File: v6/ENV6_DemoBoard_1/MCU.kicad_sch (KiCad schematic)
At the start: 50 parts, among them J101 Conn_01x03_Pin, J102 Conn_01x20_Pin, J103 Conn_01x20_Pin, U101 RP235xB, U102 W25Q16JVUXIQ, U103 Pi-Radio, Y101 KX7_QRZ

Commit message: ENV6 (test): Changes after first review
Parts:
- removed C118, C119: 0.1uF, Capacitor_SMD:C_0402_1005Metric, symbol passive:C0402
- removed D102, D103: WS2812B, LED_SMD:LED_WS2812B_PLCC4_5.0x5.0mm_P3.2mm, symbol LED:WS2812B
- removed J101: Conn_01x03_Pin, Connector_PinSocket_2.54mm:PinSocket_1x03_P2.54mm_Vertical, symbol Connector:Conn_01x03_Pin
- removed R109, R111: 10kR, Resistor_SMD:R_0402_1005Metric, symbol Device:R
- removed S101, S102, S103, S104, S105: TL3365AF180QG, ui_stuff:TL3365AF180QG, symbol TL3365AF180QG:TL3365AF180QG
- added J1: Pico Debugger (SWD), Connector_PinHeader_2.54mm:PinHeader_1x03_P2.54mm_Vertical, symbol mcu_rpi_pico:PicoDebuggerSWD
- added R1, R2: 10k, Resistor_SMD:R_0402_1005Metric, symbol Device:R
- added S1: MCU_RSTN, connectors:TACTILE-SWITCH, symbol connectors:Tactile Button
- added S2: MCU_BOOTSEL, connectors:TACTILE-SWITCH, symbol connectors:Tactile Button
- added S3, S4, S5: BTN, connectors:TACTILE-SWITCH, symbol connectors:Tactile Button
- added TP2: TestPoint, custom_library:TestPoint_Pad_D1.0mm, symbol passive:TestPoint
- C101, C102, C104, C105, C106, C107, C108, C109, C110, C120, C121: value 100nF -> 100n
- C111, C112: value 10uF -> 10µ
- C113: value 100nF -> 100n; now not fitted; now left out of the parts list
- C114, C115: value 16pF -> 16p
- C116: value 0.1uF -> 100n; now not fitted; now left out of the parts list
- C117: value 0.1uF -> 100n
- R104, U102: now not fitted; now left out of the parts list
- R106, R107: value 10kR -> 2k2
- R108: value 499R -> 750R; now not fitted; now left out of the parts list
- R110: value 10kR -> 10k; now not fitted; now left out of the parts list
- R113: value 100kR -> 100k
- Rw: renamed from R103; value 10kR -> 10k
- U101: value RP235xB -> RP2354B
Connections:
- net GND: now also J1.2 (GND), S1.1, S1.2 (1), S2.1, S2.2 (1), S3.1, S3.2 (1), S4.1, S4.2 (1), S5.1, S5.2 (1); no longer R110.1
- net IOVDD: now also R110.1, R1.1, R2.1
- net MCU_Button_1: now also R110.2, S4.3 (2), S4.4 (2)
- net MCU_Button_2: now also R1.2, S3.3 (2), S3.4 (2); no longer R110.2
- net MCU_Button_3: now also R2.2, S5.3 (2), S5.4 (2)
- net MCU_RUN: now also S1.3 (2), S1.4 (2)
- net at R104.1: now also S2.3 (2), S2.4 (2)
- net at U101.33 (SWCLK): now also J1.1 (SCLK)
- net at U101.34 (SWDIO): now also J1.3 (SDATA)
- net at D101.2 (DOUT): now also TP2.1
- no-connect marks 4 -> 3
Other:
- note added: "Add components to the FPGA board - One Clock Oscillator with enable pin - Two simple LEDs, one WS2812B - Two buttons - One RSTN button for the FPGA logic"
- note added: "I would go to only two buttons pull-ups are not necessary (we can use the pull-up inside the MCU)"
- note added: "Missing stuff - FPGA pins for programming are missing (INIT_B, RESET_B, DONE_B) - FPGA logic pins are missing (CLK, RSTN, EN_OSC, 4x GPIOs) - JTAG interface to FPGA - 1x SPI lines to FPGA (take the same like to the FPGA) - Adding Testpads to all these signals on the FPGA board"
- note added: "We do need the resistor and capacitor"
- moved on the sheet: C101, C102

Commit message: new PSU and updates
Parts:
- removed J102, J103: Conn_01x20_Pin, Connector_PinHeader_2.54mm:PinHeader_1x20_P2.54mm_Vertical, symbol Connector:Conn_01x20_Pin
- removed R2: 10k, Resistor_SMD:R_0402_1005Metric, symbol Device:R
- removed S5: BTN, connectors:TACTILE-SWITCH, symbol connectors:Tactile Button
- added J201: Conn_01x04, Connector_PinHeader_2.54mm:PinHeader_1x04_P2.54mm_Vertical, symbol Connector_Generic:Conn_01x04
- renumbered Rw to Rw1
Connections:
- net GP4/SPI0_RX: now also U101.11 (GPIO_12), U101.45 (GPIO_36); no longer U101.1 (GPIO_04)
- net GP5/SPI0_CS: now also U101.12 (GPIO_13), U101.46 (GPIO_37); no longer U101.2 (GPIO_05)
- net GP6/SPI0_SCK: now also U101.13 (GPIO_14), U101.47 (GPIO_38); no longer U101.3 (GPIO_06)
- net GP7/SPI0_TX: now also U101.14 (GPIO_15), U101.48 (GPIO_39); no longer U101.4 (GPIO_07)
- net IOVDD: no longer C111.2, C113.1, C120.1, C121.1, R106.1, R107.1, U101.61 (VREG_AVDD), U101.64 (VREG_IN), U102.8 (VCC), U103.14 (VDDIO), U103.16 (VIN)
- net MCU-FPGA: now reaches U101.16 (GPIO_16)
- net MCU-FPGA: now also U101.17 (GPIO_17), U101.18 (GPIO_18), U101.19 (GPIO_19), U101.20 (GPIO_20), U101.21 (GPIO_21), U101.22 (GPIO_22), U101.23 (GPIO_23)
- net MCU_JTAG_TMS: now reaches U101.40 (GPIO_32)
- net MCU_JTAG_TMS: now also J201.1 (Pin_1)
- net MCU_JTAG_TDI: now reaches U101.42 (GPIO_33)
- net MCU_JTAG_TDI: now also J201.2 (Pin_2)
- net MCU_JTAG_TDO: now reaches U101.43 (GPIO_34)
- net MCU_JTAG_TDO: now also J201.3 (Pin_3)
- net MCU_JTAG_TCK: now reaches U101.44 (GPIO_35)
- net MCU_JTAG_TCK: now also J201.4 (Pin_4)
- net MCU-F_M0: now reaches U101.49 (GPIO_40_ADC0)
- net MCU-F_M1: now reaches U101.52 (GPIO_41_ADC1)
- net MCU_GP42_SPI1-SCK: now reaches U101.53 (GPIO_42_ADC2)
- net MCU-F_M2: now reaches U101.54 (GPIO_43_ADC3)
- net MCU-F_DONE: now reaches U101.55 (GPIO_44_ADC4)
- net MCU-F_INIT_B: now reaches U101.56 (GPIO_45_ADC5)
- net MCU-F_PROGRAM_B: now reaches U101.57 (GPIO_46_ADC6)
- net MCU-F_RESET: now reaches U101.58 (GPIO_47_ADC7)
- net PAC2_GPIO: now reaches U101.6 (GPIO_08)
- net EN_OSC: now reaches U101.9 (GPIO_11)
- net MCU_Button_3 renamed PAC1_GPIO
- net PAC_PWRDN renamed BQ_TS/MR
- new net 3V3_MCU_FLASH: C113.1, U102.8 (VCC)
- new net 3V3_Pi_Radio: C120.1, C121.1, U103.14 (VDDIO), U103.16 (VIN)
- new net LP_EN1: U101.2 (GPIO_05)
- new net LP_EN2: U101.1 (GPIO_04)
- new net LP_NRST: U101.3 (GPIO_06)
- new net LP_nINT: U101.4 (GPIO_07)
- new net VCC_MCU: C111.2, R106.1, R107.1, U101.61 (VREG_AVDD), U101.64 (VREG_IN)
- no-connect marks 3 -> 5
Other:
- note added: "DirtyJTAG For FPGA"
- note added: "FPGA Programming"
- note added: "GPIOs to FPGA"
- note added: "Pi Radio WiFi"
- note added: "SPI 0 for microSD card"
- note added: "SPI 1 to FPGA Board"
- moved on the sheet: R1, R110, S3, S4

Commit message: Changes after second rev of ENV6 test
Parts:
- removed C116: 100n, Capacitor_SMD:C_0402_1005Metric, symbol Device:C
- removed J201: Conn_01x04, Connector_PinHeader_2.54mm:PinHeader_1x04_P2.54mm_Vertical, symbol Connector_Generic:Conn_01x04
- removed R1, R110: 10k, Resistor_SMD:R_0402_1005Metric, symbol Device:R
- removed R108: 750R, Resistor_SMD:R_0402_1005Metric, symbol Device:R
- removed S3: BTN, connectors:TACTILE-SWITCH, symbol connectors:Tactile Button
- C11: renamed from C111; value 10µ -> 10u
- C12: renamed from C112; value 10µ -> 10u
- C3: renamed from C103; value 100nF -> 100n
- J1: now not fitted; now left out of the parts list
- R1: renamed from R106; value 2k2 -> 5k1
- R2: renamed from R107; value 2k2 -> 5k1
- R6: renamed from R113; value 100k -> 10k
- R8: renamed from R104; value 2kR -> 750R; now fitted; now in the parts list
- S3: renamed from S2; now fitted; now in the parts list
- renumbered C101 to C1, C110 to C10, C117 to C13, C113 to C14, C120 to C15, C121 to C16, C114 to C17, C115 to C18, C102 to C2, C104 to C4, C105 to C5, C106 to C6, C107 to C7, C108 to C8, C109 to C9, D101 to D1, L101 to L1, R101 to R3, R102 to R4, R112 to R5, Rw1 to R7, R105 to R9, S4 to S2, TP2 to TP1, U101 to U1, U103 to U2, U102 to U3, Y101 to Y1
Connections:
- net MCU_Button_2 is gone; now on net MCU_LEDS: U1.38 (GPIO_30)
- net PAC1_GPIO is gone; now on net MCU_Button_1: U1.39 (GPIO_31)
- net VCC_MCU is gone; now on net VDDD_MCU: C11.2, R1.1, R2.1, U1.61 (VREG_AVDD), U1.64 (VREG_IN)
- net MCU-FPGA: no longer U1.21 (GPIO_21), U1.22 (GPIO_22), U1.23 (GPIO_23)
- net MCU_Button_1: no longer U1.37 (GPIO_29)
- net MCU_LEDS: no longer U1.36 (GPIO_28)
- net WL_EN: now also U1.23 (GPIO_23); no longer U1.28 (GPIO_27)
- net WL_SCLK: now also U1.37 (GPIO_29); no longer U1.27 (GPIO_26)
- net 3V3_MCU_FLASH renamed VDDD_FLASH
- net VDDD_FLASH: now also R7.1
- net 3V3_Pi_Radio renamed VDDD_RADIO
- net BQ_INT: no longer names the net of U1.79 (GPIO_02)
- net BQ_TS/MR: no longer names the net of U1.80 (GPIO_03)
- net EN_OSC: no longer names the net of U1.9 (GPIO_11)
- net IOVDD renamed VDDD_MCU
- net VDDD_MCU: no longer R7.1
- net LP_EN1: no longer names the net of U1.2 (GPIO_05)
- net LP_EN2: no longer names the net of U1.1 (GPIO_04)
- net LP_NRST: no longer names the net of U1.3 (GPIO_06)
- net LP_nINT: no longer names the net of U1.4 (GPIO_07)
- net MCU-F_M0: no longer names the net of U1.49 (GPIO_40_ADC0)
- net MCU-F_M1: no longer names the net of U1.52 (GPIO_41_ADC1)
- net MCU-F_M2: no longer names the net of U1.54 (GPIO_43_ADC3)
- net MCU_GP42_SPI1-SCK: no longer names the net of U1.53 (GPIO_42_ADC2)
- net PAC2_GPIO: no longer names the net of U1.6 (GPIO_08)
- new net MCU-FPGA_EN_OSC: U1.22 (GPIO_22)
- new net MCU-FPGA_NRST_LOGIC: U1.21 (GPIO_21)
- no-connect marks 5 -> 3
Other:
- note added: "3, MCU RP2354B"
- note added: "Infos for FPGA board - Adding Testpads to all these signals on the FPGA board - Add ADC for identifying which FPGA board is connected via voltage divider - Move F_Mx pins to fpga directly (configure flash fpga interaction) using resistors - One Clock Oscillator with enable pin - One RSTN button for the FPGA logic - Bring unused GPIO to connector (for application)"
- note added: "if not work, replace with 100k"
- note added: "power supply voltage 3.5 - 5.3 V"
- note removed: "1, MCU RP2354B"
- note removed: "Add components to the FPGA board - One Clock Oscillator with enable pin - Two simple LEDs, one WS2812B - Two buttons - One RSTN button for the FPGA logic"
- note removed: "I would go to only two buttons pull-ups are not necessary (we can use the pull-up inside the MCU)"
- note removed: "Missing stuff - FPGA pins for programming are missing (INIT_B, RESET_B, DONE_B) - FPGA logic pins are missing (CLK, RSTN, EN_OSC, 4x GPIOs) - JTAG interface to FPGA - 1x SPI lines to FPGA (take the same like to the FPGA) - Adding Testpads to all these signals on the FPGA board"
- note removed: "WS2812B power supply voltage 3.5 - 5.3 V"
- note removed: "We do need the resistor and capacitor"
- moved on the sheet: C14, C17, C18, R1, R2, R7, R9, S1, S2, U3, Y1

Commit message: added comments
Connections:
- removed net MCU-FPGA: U1.16 (GPIO_16), U1.17 (GPIO_17), U1.18 (GPIO_18), U1.19 (GPIO_19), U1.20 (GPIO_20)
- new net MCU16-FPGA: U1.16 (GPIO_16)
- new net MCU17-FPGA: U1.17 (GPIO_17)
- new net MCU18-FPGA: U1.18 (GPIO_18)
- new net MCU19-FPGA: U1.19 (GPIO_19)
- new net MCU20-FPGA: U1.20 (GPIO_20)
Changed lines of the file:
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@@
 	(text "FPGA \nProgramming"
 		(exclude_from_sim no)
-		(at 168.402 180.34 0)
+		(at 168.91 179.07 0)
 		(effects
 			(font
@@
 	(text "if not work, \nreplace with 100k"
 		(exclude_from_sim no)
-		(at 268.986 151.13 0)
+		(at 266.192 151.892 0)
 		(effects
 			(font
@@
 	(text "DirtyJTAG\nFor FPGA"
 		(exclude_from_sim no)
-		(at 160.528 145.288 0)
+		(at 160.528 143.51 0)
 		(effects
 			(font
@@
 	(polyline
 		(pts
-			(xy 161.29 185.42) (xy 162.56 185.42)
+			(xy 161.798 184.15) (xy 163.068 184.15)
 		)
 		(stroke
@@
 	(polyline
 		(pts
-			(xy 153.035 140.335) (xy 154.305 140.335)
+			(xy 153.035 137.16) (xy 154.305 137.16)
 		)
 		(stroke
@@
 	(polyline
 		(pts
-			(xy 161.925 175.26) (xy 162.56 175.26)
+			(xy 162.433 173.99) (xy 163.068 173.99)
 		)
 		(stroke
@@
 	(polyline
 		(pts
-			(xy 161.925 175.26) (xy 161.925 185.42)
+			(xy 162.433 173.99) (xy 162.433 184.15)
 		)
 		(stroke
@@
 	(polyline
 		(pts
-			(xy 161.29 175.26) (xy 162.56 175.26)
+			(xy 161.798 173.99) (xy 163.068 173.99)
 		)
 		(stroke
@@
 	(polyline
 		(pts
-			(xy 153.67 140.335) (xy 153.67 149.86)
+			(xy 153.67 137.16) (xy 153.67 149.86)
 		)
 		(stroke
@@
 		)
 	)
-	(global_label "MCU-FPGA"
+	(global_label "MCU16-FPGA"
 		(shape bidirectional)
 		(at 137.16 96.52 0)
@@
 		)
 		(property "Intersheetrefs" "${INTERSHEET_REFS}"
-			(at 151.598 96.52 0)
+			(at 154.017 96.52 0)
 			(effects
 				(font
@@
 		)
 	)
-	(global_label "MCU-FPGA"
+	(global_label "MCU18-FPGA"
 		(shape bidirectional)
 		(at 137.16 101.6 0)
@@
 		)
 		(property "Intersheetrefs" "${INTERSHEET_REFS}"
-			(at 151.598 101.6 0)
+			(at 154.017 101.6 0)
 			(effects
 				(font
@@
 		)
 	)
-	(global_label "MCU-FPGA"
+	(global_label "MCU19-FPGA"
 		(shape bidirectional)
 		(at 137.16 104.14 0)
@@
 		)
 		(property "Intersheetrefs" "${INTERSHEET_REFS}"
-			(at 151.598 104.14 0)
+			(at 154.017 104.14 0)
 			(effects
 				(font
@@
 		)
 	)
-	(global_label "MCU-FPGA"
+	(global_label "MCU20-FPGA"
 		(shape bidirectional)
 		(at 137.16 106.68 0)
@@
 		)
 		(property "Intersheetrefs" "${INTERSHEET_REFS}"
-			(at 151.598 106.68 0)
+			(at 154.017 106.68 0)
 			(effects
 				(font
@@
 		)
 	)
-	(global_label "MCU-FPGA"
+	(global_label "MCU17-FPGA"
 		(shape bidirectional)
 		(at 137.16 99.06 0)
@@
 		)
 		(property "Intersheetrefs" "${INTERSHEET_REFS}"
-			(at 151.598 99.06 0)
+			(at 154.017 99.06 0)
 			(effects
 				(font

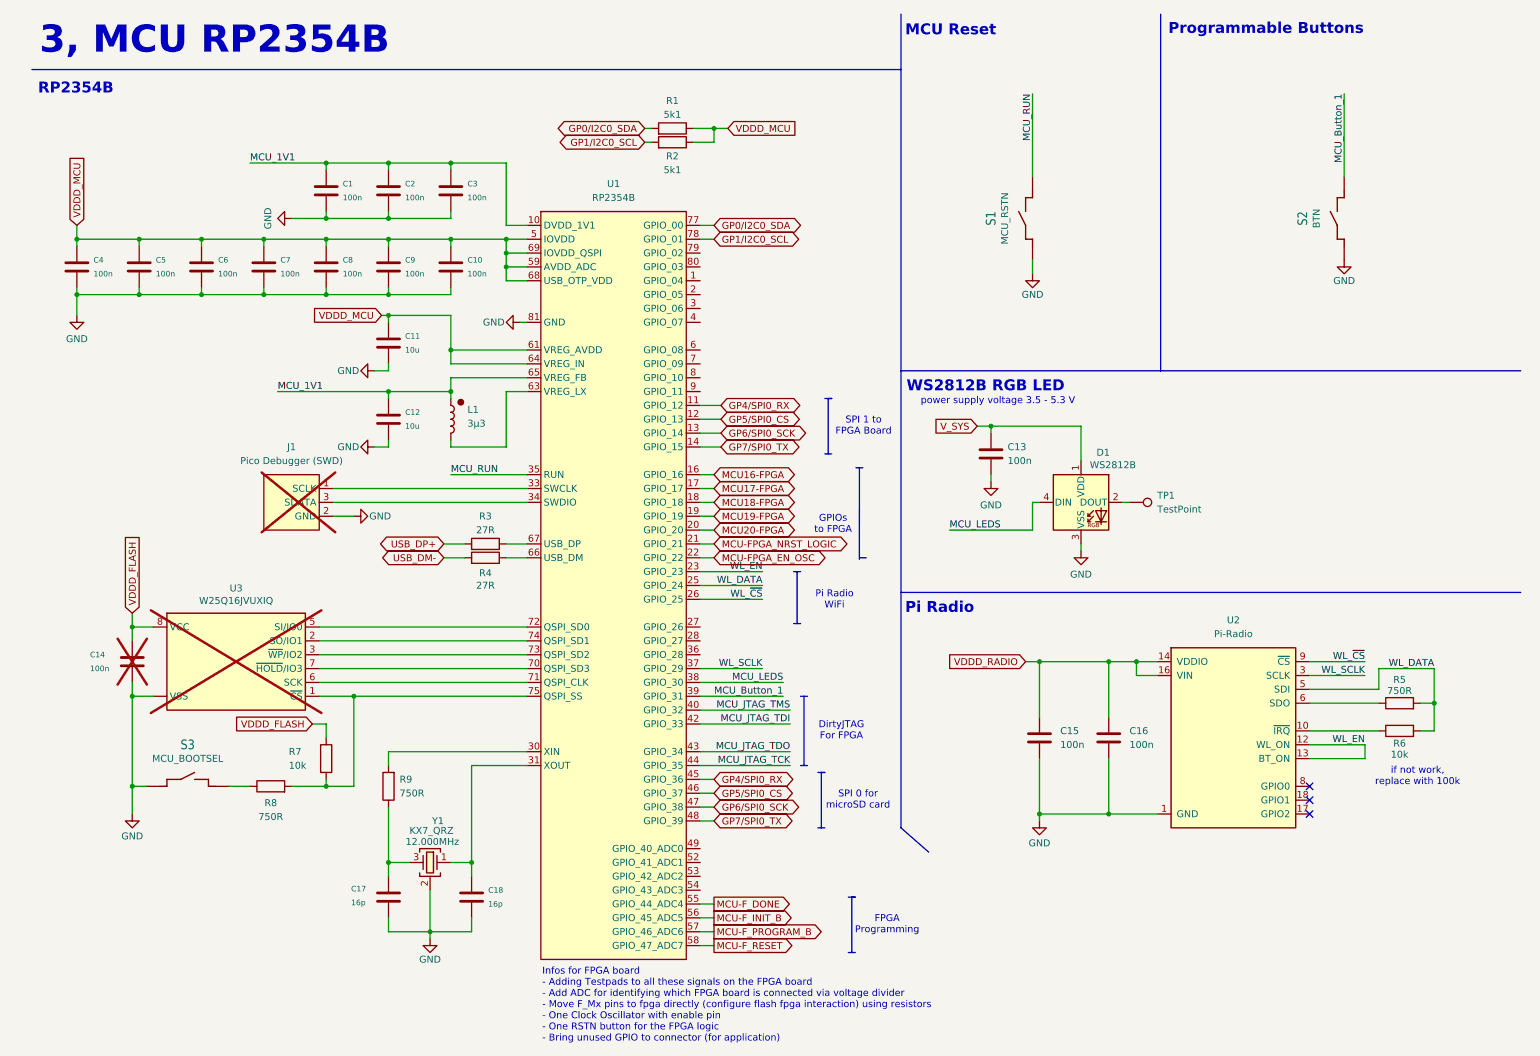
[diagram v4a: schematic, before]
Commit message: update Demoboard and add GateMateA11 board
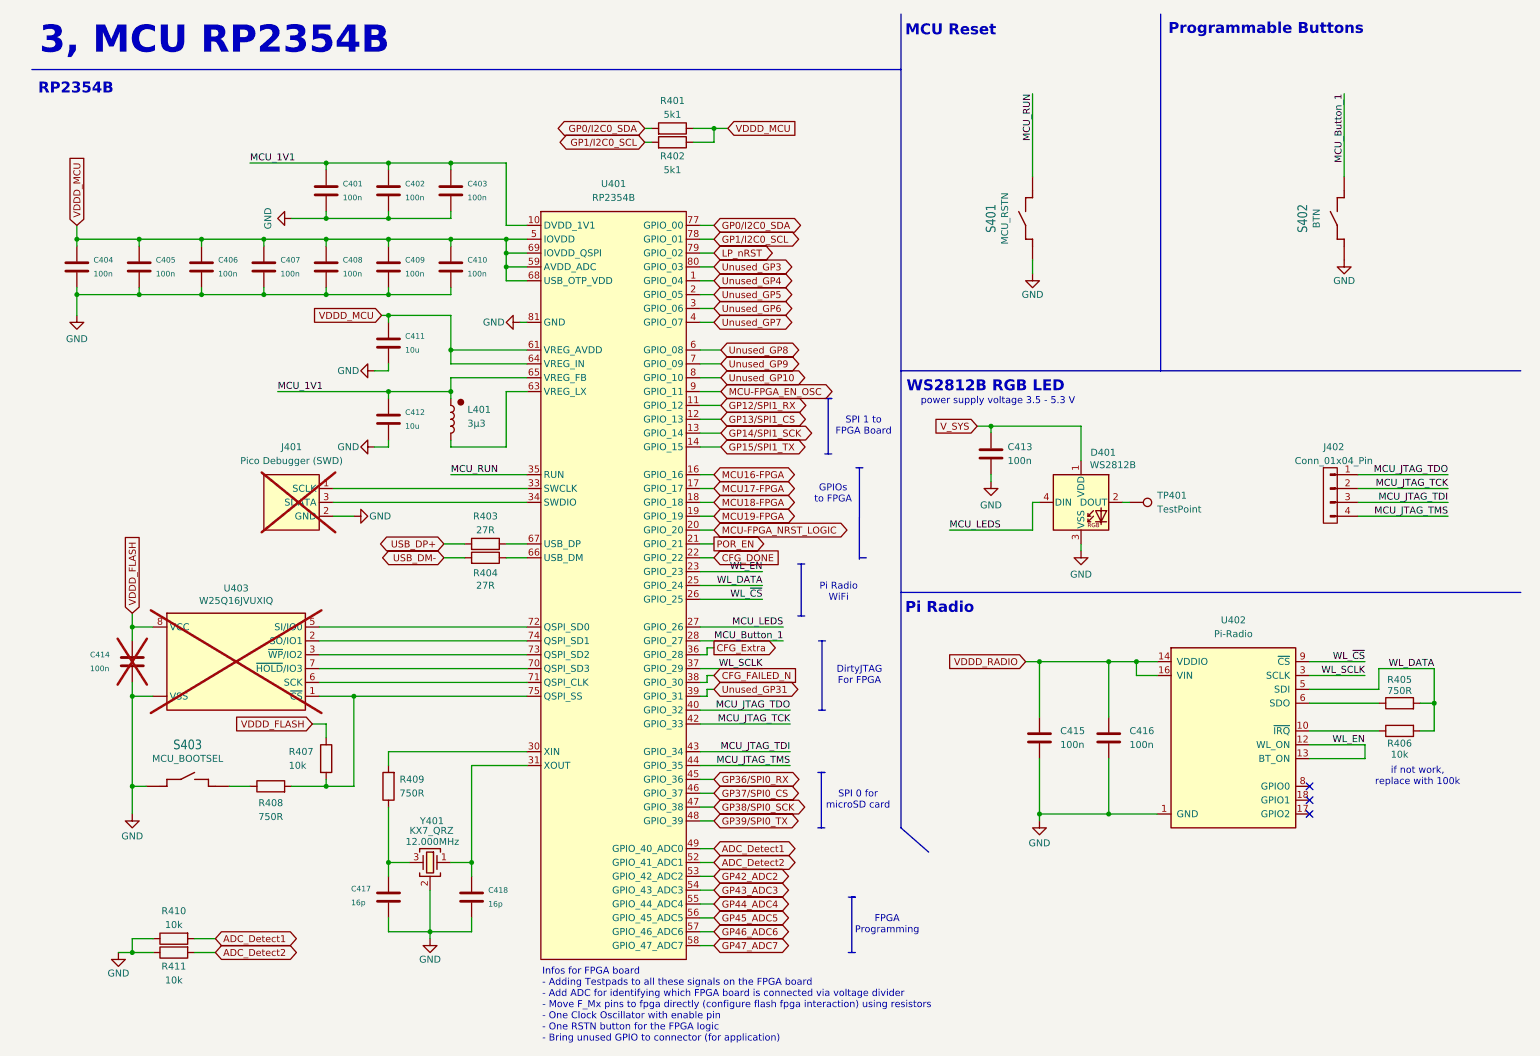
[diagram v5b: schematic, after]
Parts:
- added J402: Conn_01x04_Pin, Connector_PinSocket_2.00mm:PinSocket_1x04_P2.00mm_Vertical, symbol Connector:Conn_01x04_Pin
- added R410, R411: 10k, Resistor_SMD:R_0402_1005Metric, symbol Device:R
- renumbered C1 to C401, C2 to C402, C3 to C403, C4 to C404, C5 to C405, C6 to C406, C7 to C407, C8 to C408, C9 to C409, C10 to C410, C11 to C411, C12 to C412, C13 to C413, C14 to C414, C15 to C415, C16 to C416, C17 to C417, C18 to C418, D1 to D401, J1 to J401, L1 to L401, R1 to R401, R2 to R402, R3 to R403, R4 to R404, R5 to R405, R6 to R406, R7 to R407, R8 to R408, R9 to R409, S1 to S401, S2 to S402, S3 to S403, TP1 to TP401, U1 to U401, U2 to U402, U3 to U403, Y1 to Y401
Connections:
- net MCU20-FPGA is gone; now on net MCU-FPGA_NRST_LOGIC: U401.20 (GPIO_20)
- net GND: now also R410.1, R411.1
- net MCU-FPGA_EN_OSC: now also U401.9 (GPIO_11); no longer U401.22 (GPIO_22)
- net MCU-FPGA_NRST_LOGIC: no longer U401.21 (GPIO_21)
- net MCU_Button_1: now also U401.28 (GPIO_27); no longer U401.39 (GPIO_31)
- net MCU_JTAG_TCK: now also U401.42 (GPIO_33), J402.2 (Pin_2); no longer U401.44 (GPIO_35)
- net MCU_JTAG_TDI: now also U401.43 (GPIO_34), J402.3 (Pin_3); no longer U401.42 (GPIO_33)
- net MCU_JTAG_TDO: now also U401.40 (GPIO_32), J402.1 (Pin_1); no longer U401.43 (GPIO_34)
- net MCU_JTAG_TMS: now also U401.44 (GPIO_35), J402.4 (Pin_4); no longer U401.40 (GPIO_32)
- net MCU_LEDS: now also U401.27 (GPIO_26); no longer U401.38 (GPIO_30)
- net Unused_GP4: now reaches U401.1 (GPIO_04)
- net Unused_GP5: now reaches U401.2 (GPIO_05)
- net Unused_GP6: now reaches U401.3 (GPIO_06)
- net CFG_Extra: now reaches U401.36 (GPIO_28)
- net Unused_GP7: now reaches U401.4 (GPIO_07)
- net ADC_Detect1: now reaches U401.49 (GPIO_40_ADC0)
- net ADC_Detect1: now also R410.2
- net ADC_Detect2: now reaches U401.52 (GPIO_41_ADC1)
- net ADC_Detect2: now also R411.2
- net GP42_ADC2: now reaches U401.53 (GPIO_42_ADC2)
- net GP43_ADC3: now reaches U401.54 (GPIO_43_ADC3)
- net Unused_GP8: now reaches U401.6 (GPIO_08)
- net Unused_GP9: now reaches U401.7 (GPIO_09)
- net LP_nRST: now reaches U401.79 (GPIO_02)
- net Unused_GP10: now reaches U401.8 (GPIO_10)
- net Unused_GP3: now reaches U401.80 (GPIO_03)
- net GP4/SPI0_RX renamed GP12/SPI1_RX
- net GP12/SPI1_RX: no longer U401.45 (GPIO_36)
- net GP5/SPI0_CS renamed GP13/SPI1_CS
- net GP13/SPI1_CS: no longer U401.46 (GPIO_37)
- net GP6/SPI0_SCK renamed GP14/SPI1_SCK
- net GP14/SPI1_SCK: no longer U401.47 (GPIO_38)
- net GP7/SPI0_TX renamed GP15/SPI1_TX
- net GP15/SPI1_TX: no longer U401.48 (GPIO_39)
- net MCU-F_DONE renamed GP44_ADC4
- net MCU-F_INIT_B renamed GP45_ADC5
- net MCU-F_PROGRAM_B renamed GP46_ADC6
- net MCU-F_RESET renamed GP47_ADC7
- new net CFG_DONE: U401.22 (GPIO_22)
- new net CFG_FAILED_N: U401.38 (GPIO_30)
- new net GP36/SPI0_RX: U401.45 (GPIO_36)
- new net GP37/SPI0_CS: U401.46 (GPIO_37)
- new net GP38/SPI0_SCK: U401.47 (GPIO_38)
- new net GP39/SPI0_TX: U401.48 (GPIO_39)
- new net POR_EN: U401.21 (GPIO_21)
- new net Unused_GP31: U401.39 (GPIO_31)
